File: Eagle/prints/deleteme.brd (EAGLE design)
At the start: 4 parts

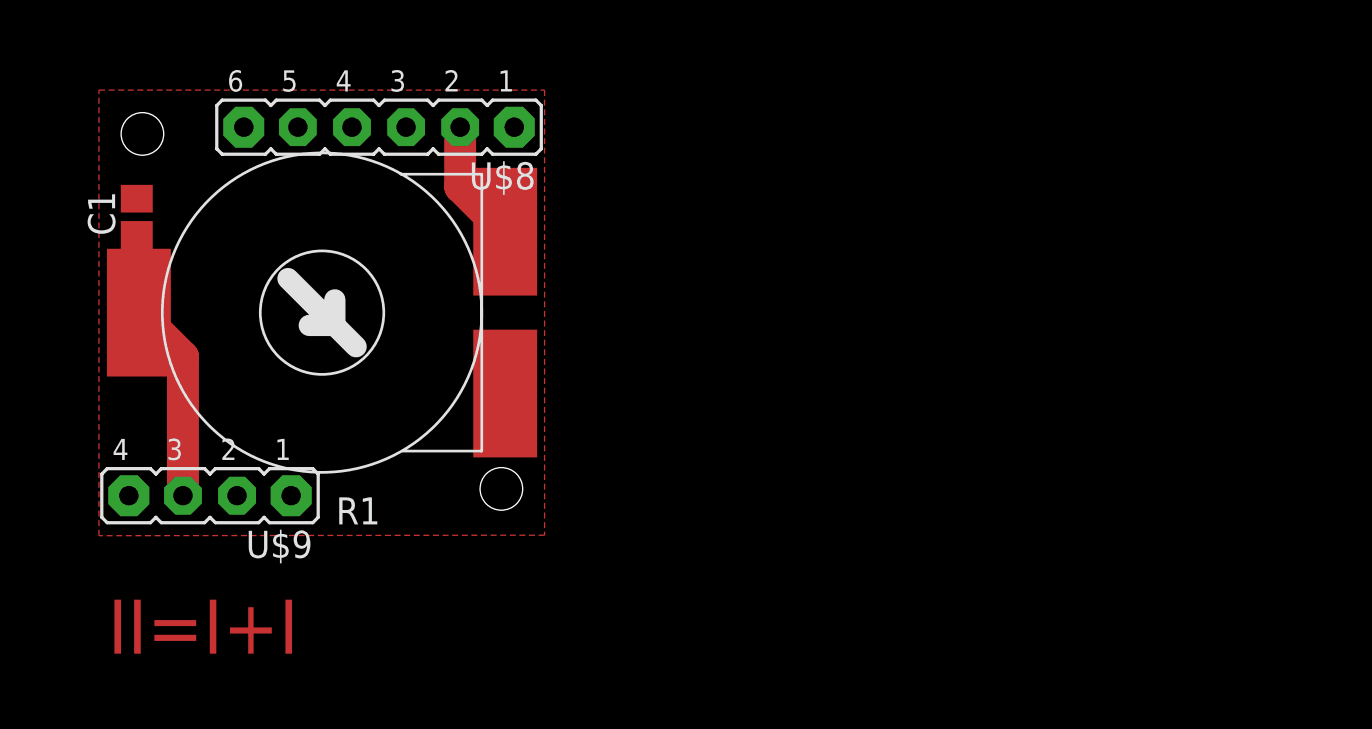
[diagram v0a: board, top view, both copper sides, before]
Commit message: eagle adjustment for the Jíťa version
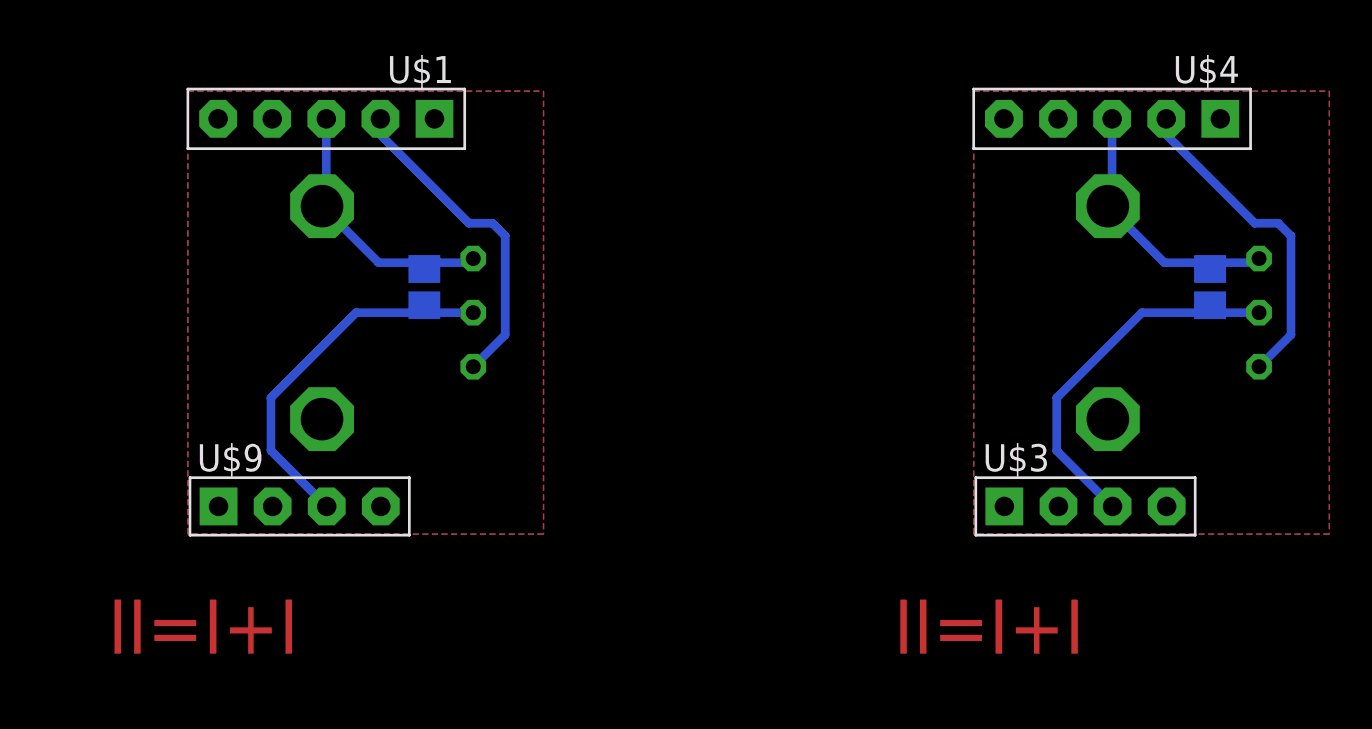
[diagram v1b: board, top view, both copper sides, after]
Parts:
- removed R1: 10 k, !stavebnice03:R-TRIM
- removed U$8: JUMPER6M, !stavebnice03:JUMPER6M
- added C2: 100 nF, resistor:C0805
- added U$1, U$4: JUMPER5M, !stavebnice03:JUMPER5M
- added U$2, U$5: POTENTIOMETER-RK09, !stavebnice03:POTENTIOMETER-RK09
- added U$3: JUMPER4M, !stavebnice03:JUMPER4M
- moved C1 13.9 mm to (15.3, 11.7), flipped to the bottom
- moved U$9 4.24 mm to (9.45, 1.40), turned to 0 degrees
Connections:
- new net GND1: C2.2, U$4.3, U$5.1, U$5.GND1, U$5.GND2
- new net N$3: C2.1, U$3.3, U$5.2
- new net N$4: U$4.2, U$5.3
- net GND: now also U$1.3, U$2.1, U$2.GND1, U$2.GND2; no longer R1.1, U$8.1, U$8.3, U$8.4, U$8.5, U$8.6, U$9.1, U$9.2, U$9.4
- net N$1: now also U$2.2; no longer R1.2
- net N$2: now also U$1.2, U$2.3; no longer R1.3, U$8.2
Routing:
- net N$3: track 0.00 -> 17.7 mm
- net N$4: track 0.00 -> 15.4 mm
- net GND1: track 0.00 -> 12.9 mm
- net GND: track 0.00 -> 12.9 mm
- net N$2: track 5.78 -> 15.4 mm
- net N$1: track 13.1 -> 17.7 mm
- added copper zone on layer 16, net GND
- added copper zone on layer 1, net GND1
- added copper zone on layer 16, net GND1
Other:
- board text added: "potentiometer"
- board text removed: "trim for 5 pin interface v1"
